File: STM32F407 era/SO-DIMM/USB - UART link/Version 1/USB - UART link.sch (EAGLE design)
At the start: 71 parts, among them J1 22-27-2031-03, J2 22-27-2031-03, J3 22-27-2041-04, J4 22-27-2031-03, Q1 6MHz, Q2 12MHz, Q3 12MHz, U1 TUSB2036VF, U3 MAX232AEWE+, U5 SN75240PWG4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

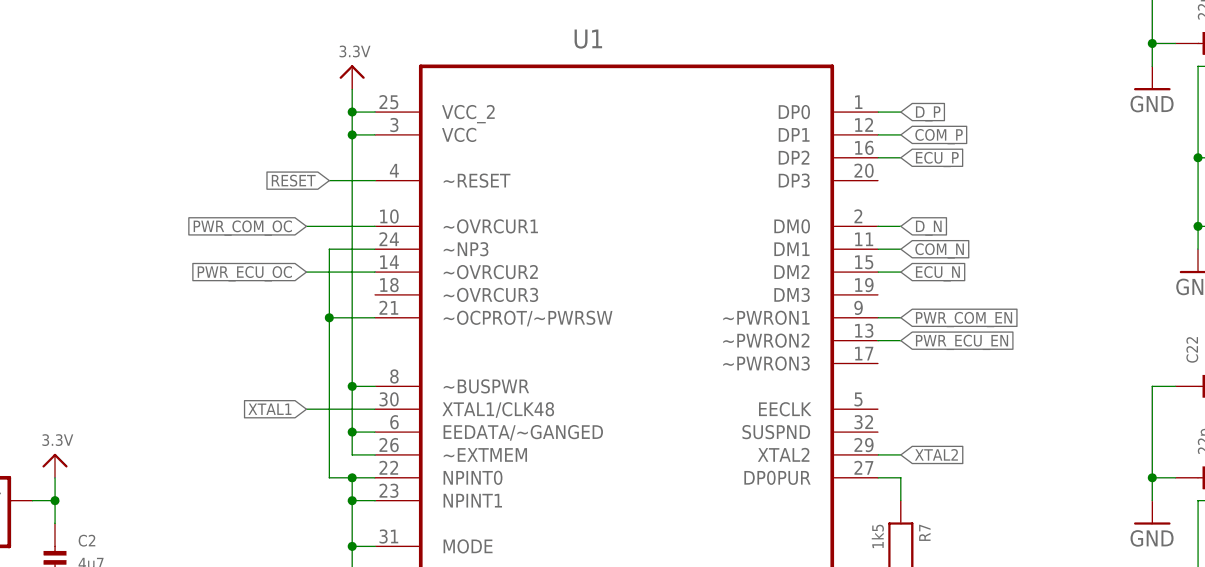
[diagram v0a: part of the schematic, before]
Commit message: COM/TC RC1 done
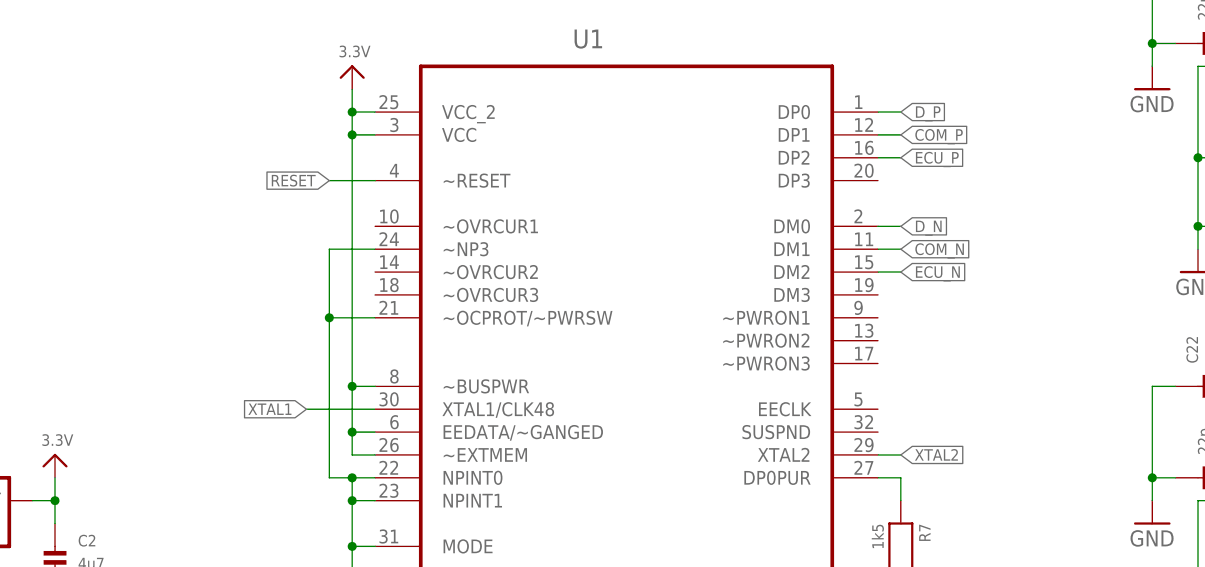
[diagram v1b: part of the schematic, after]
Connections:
- removed net PWR_COM_EN: U1.~PWRON1
- removed net PWR_COM_OC: U1.~OVRCUR1
- removed net PWR_ECU_EN: U1.~PWRON2
- removed net PWR_ECU_OC: U1.~OVRCUR2
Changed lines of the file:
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@@
-</segment>
-</net>
-<net name="PWR_COM_EN" class="0">
-<segment>
-<pinref part="U1" gate="A" pin="~PWRON1"/>
-<wire x1="15.24" y1="83.82" x2="12.7" y2="83.82" width="0.1524" layer="91"/>
-<label x="15.24" y="83.82" size="1.27" layer="95" xref="yes"/>
-</segment>
-</net>
-<net name="PWR_ECU_EN" class="0">
-<segment>
-<pinref part="U1" gate="A" pin="~PWRON2"/>
-<wire x1="15.24" y1="81.28" x2="12.7" y2="81.28" width="0.1524" layer="91"/>
-<label x="15.24" y="81.28" size="1.27" layer="95" xref="yes"/>
-</segment>
-</net>
-<net name="PWR_COM_OC" class="0">
-<segment>
-<pinref part="U1" gate="A" pin="~OVRCUR1"/>
-<wire x1="-50.8" y1="93.98" x2="-43.18" y2="93.98" width="0.1524" layer="91"/>
-<label x="-50.8" y="93.98" size="1.27" layer="95" rot="R180" xref="yes"/>
-</segment>
-</net>
-<net name="PWR_ECU_OC" class="0">
-<segment>
-<pinref part="U1" gate="A" pin="~OVRCUR2"/>
-<wire x1="-50.8" y1="88.9" x2="-43.18" y2="88.9" width="0.1524" layer="91"/>
-<label x="-50.8" y="88.9" size="1.27" layer="95" rot="R180" xref="yes"/>
 </segment>
 </net>
@@
 </sheet>
 </sheets>
+<errors>
+</errors>
 </schematic>
 </drawing>

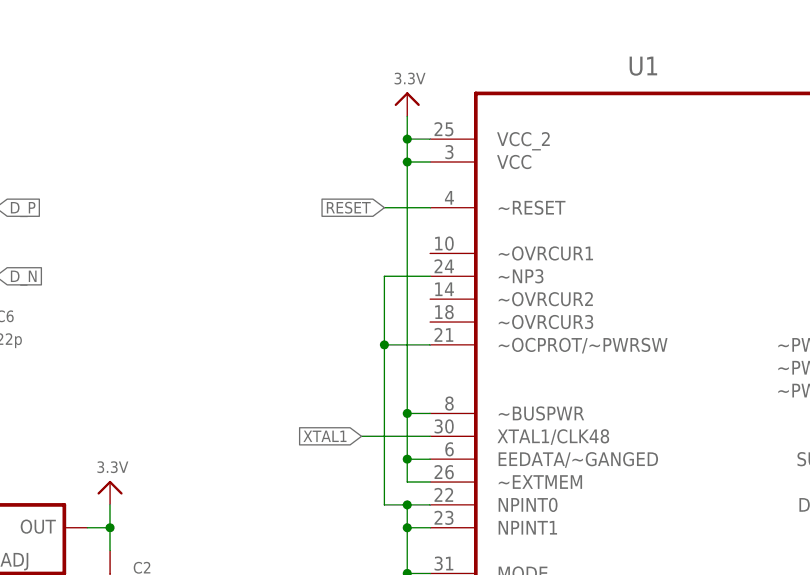
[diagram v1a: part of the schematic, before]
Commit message: last end changes on boards
Dev board
- Added 8 LED for ekstra debugging feature
- fixed Tvalue silkscreen
-

COM/TC
- fixed connections om P-channel RPP
- 12V from debug changed to include RPP and fuse

Dash
- fixed connections om P-channel RPP
- 12V from debug changed to include RPP and fuse

debug
- Added "ohm/not ohm to silkscreen
- Added BNC connectors for CAN

and much much more
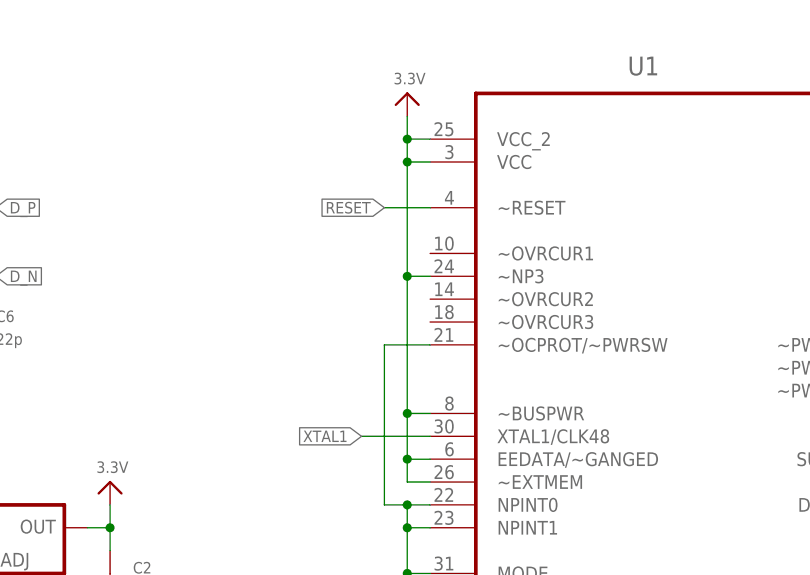
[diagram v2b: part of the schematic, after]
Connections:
- net 3.3V: now also U1.~NP3
- net GND: no longer U1.~NP3
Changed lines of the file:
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@@
 <wire x1="-45.72" y1="66.04" x2="-45.72" y2="63.5" width="0.1524" layer="91"/>
 <junction x="-45.72" y="63.5"/>
-<pinref part="U1" gate="A" pin="~NP3"/>
-<wire x1="-43.18" y1="91.44" x2="-48.26" y2="91.44" width="0.1524" layer="91"/>
-<wire x1="-48.26" y1="91.44" x2="-48.26" y2="83.82" width="0.1524" layer="91"/>
 <wire x1="-48.26" y1="83.82" x2="-48.26" y2="66.04" width="0.1524" layer="91"/>
 <wire x1="-48.26" y1="66.04" x2="-45.72" y2="66.04" width="0.1524" layer="91"/>
@@
 <pinref part="U1" gate="A" pin="~OCPROT/~PWRSW"/>
 <wire x1="-43.18" y1="83.82" x2="-48.26" y2="83.82" width="0.1524" layer="91"/>
-<junction x="-48.26" y="83.82"/>
 </segment>
 <segment>
@@
 <pinref part="U1" gate="A" pin="~BUSPWR"/>
 <wire x1="-43.18" y1="76.2" x2="-45.72" y2="76.2" width="0.1524" layer="91"/>
-<wire x1="-45.72" y1="76.2" x2="-45.72" y2="104.14" width="0.1524" layer="91"/>
+<wire x1="-45.72" y1="76.2" x2="-45.72" y2="91.44" width="0.1524" layer="91"/>
 <junction x="-45.72" y="104.14"/>
 <pinref part="U1" gate="A" pin="EEDATA/~GANGED"/>
+<wire x1="-45.72" y1="91.44" x2="-45.72" y2="104.14" width="0.1524" layer="91"/>
 <wire x1="-43.18" y1="71.12" x2="-45.72" y2="71.12" width="0.1524" layer="91"/>
 <wire x1="-45.72" y1="71.12" x2="-45.72" y2="76.2" width="0.1524" layer="91"/>
@@
 <wire x1="-45.72" y1="68.58" x2="-45.72" y2="71.12" width="0.1524" layer="91"/>
 <junction x="-45.72" y="71.12"/>
+<pinref part="U1" gate="A" pin="~NP3"/>
+<wire x1="-45.72" y1="91.44" x2="-43.18" y2="91.44" width="0.1524" layer="91"/>
+<junction x="-45.72" y="91.44"/>
 </segment>
 <segment>
